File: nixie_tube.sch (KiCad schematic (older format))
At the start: 22 parts, among them J1 Conn_01x06_Male, J11 dc003a, J2 Conn_01x06_Female, J3 Conn_01x01_Male, J4 Conn_01x01_Female, Q1 SS8550, Q2 FQD5N60C, Q3 Q_NPN_BCE, Q4 AO3400, U1 MC34063

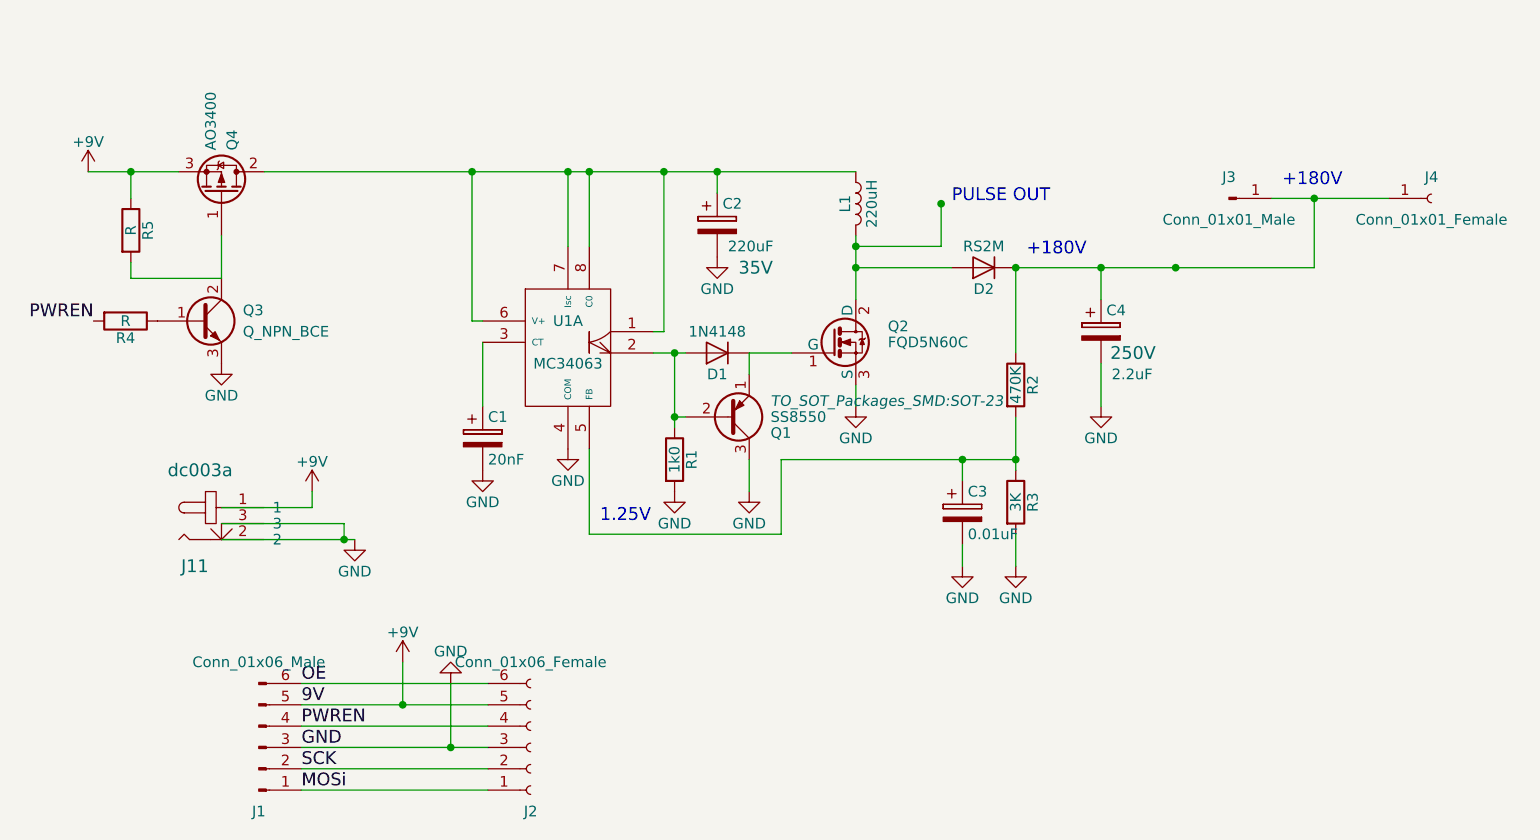
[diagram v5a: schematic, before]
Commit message: reallocate space for 4 m3 pins
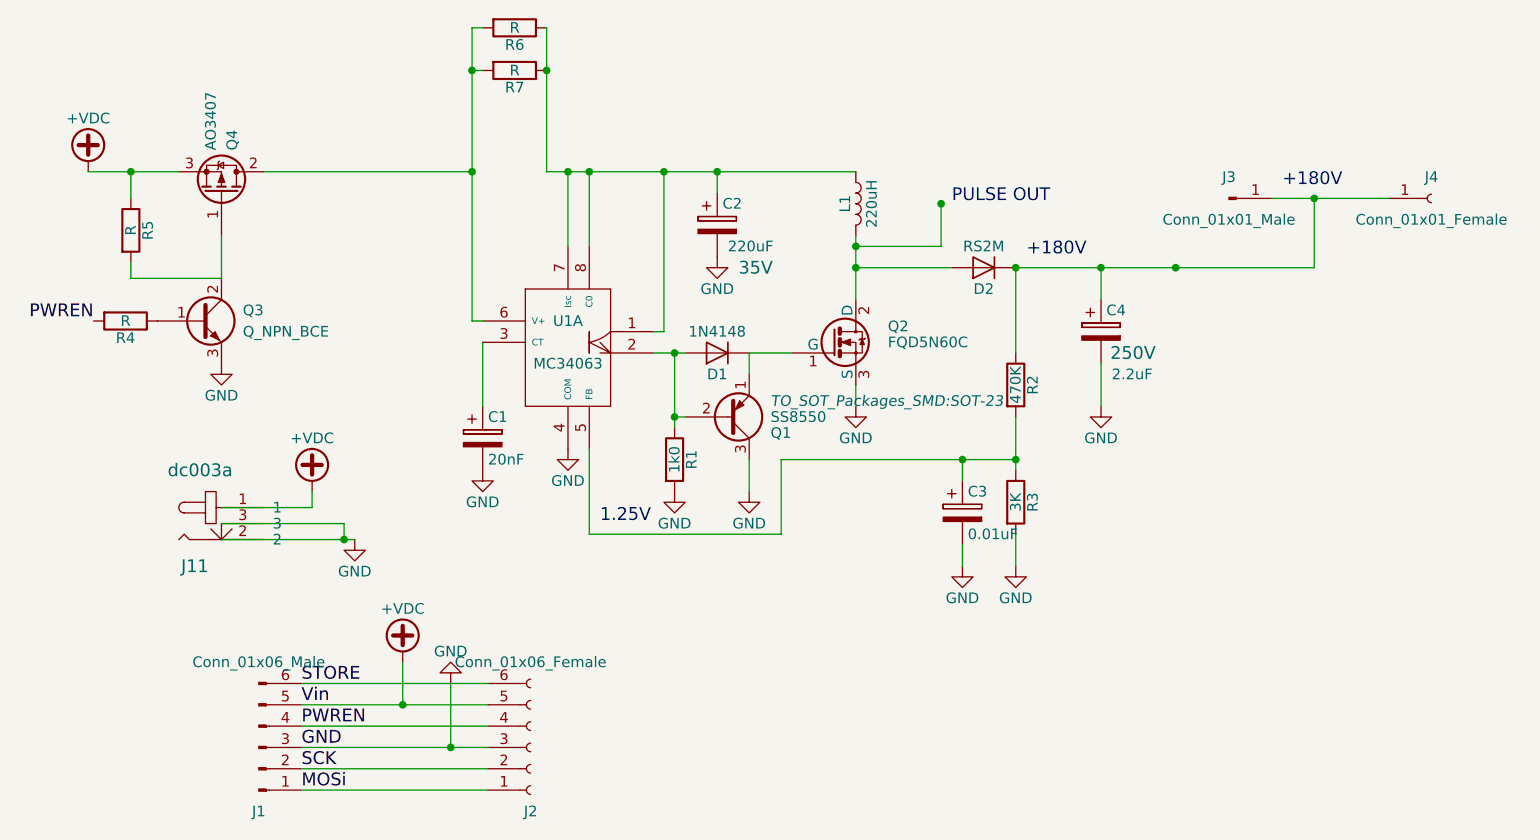
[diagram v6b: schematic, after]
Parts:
- added R6, R7: R, nixie-tube-fp:R_2512_0805, symbol R
- C4: footprint Capacitors_THT:CP_Radial_D8.0mm_P2.50mm -> nixie-tube-fp:CP_RADIAL_and_mlcc
- Q4: value AO3400 -> AO3407
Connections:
- net at C2.1, L1.1, U1.1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: now also R6.1, R7.1; no longer Q4.2 (D), U1.6 (V+)
- net +9V renamed +VDC
- net OE renamed STORE
- new net: Q4.2 (D), R6.2, R7.2, U1.6 (V+)
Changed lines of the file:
@@
 F 0 "C4" H 5975 3050 50  0000 L CNN
 F 1 "2.2uF" H 6000 2750 50  0000 L CNN
-F 2 "Capacitors_THT:CP_Radial_D8.0mm_P2.50mm" H 5988 2800 50  0001 C CNN
+F 2 "nixie-tube-fp:CP_RADIAL_and_mlcc" H 5988 2800 50  0001 C CNN
 F 3 "" H 5950 2950 50  0000 C CNN
 F 4 "250V" H 6100 2850 60  0000 C CNN "voltage"
@@
 $EndComp
 Text Label 2200 4700 0    60   ~ 0
-9V
+Vin
 Text Label 2200 4800 0    60   ~ 0
 PWREN
@@
 MOSi
 $Comp
-L +9V #PWR011
-U 1 1 59E5E8EF
-P 2250 3700
-F 0 "#PWR011" H 2250 3550 50  0001 C CNN
-F 1 "+9V" H 2250 3840 50  0000 C CNN
-F 2 "" H 2250 3700 50  0001 C CNN
-F 3 "" H 2250 3700 50  0001 C CNN
-	1    2250 3700
-	1    0    0    -1
-$EndComp
-Wire Wire Line
-	3450 2200 3450 2550
-Connection ~ 3450 2200
-Wire Wire Line
-	3850 2950 3900 2950
-Wire Wire Line
-	3900 2950 3900 2200
-Connection ~ 3550 2200
-Wire Wire Line
-	4150 2200 4150 2300
-Connection ~ 3900 2200
-Connection ~ 4150 2200
-Wire Wire Line
-	5550 2650 5550 3050
-Wire Wire Line
-	3550 3900 4450 3900
-Wire Wire Line
-	3550 3500 3550 3900
-Wire Wire Line
-	3850 3050 4000 3050
-Wire Wire Line
-	4300 3050 4300 3150
-Wire Wire Line
-	3950 3050 3950 3400
-Wire Wire Line
-	3950 3350 4000 3350
-Connection ~ 3950 3050
-Connection ~ 3950 3350
-Wire Wire Line
-	3050 3000 3050 3300
-Wire Wire Line
-	3000 2200 3000 2900
-Wire Wire Line
-	3000 2900 3050 2900
-Connection ~ 3000 2200
-Wire Wire Line
-	4800 3200 4800 3300
-Wire Wire Line
-	4300 3050 4500 3050
-Wire Wire Line
-	4800 2500 4800 2800
-Wire Wire Line
-	4800 2650 5250 2650
-Connection ~ 4800 2650
-Wire Wire Line
-	4800 2550 5200 2550
-Wire Wire Line
-	5200 2550 5200 2350
-Connection ~ 4800 2550
-Connection ~ 5200 2350
-Wire Wire Line
-	4450 3900 4450 3550
-Wire Wire Line
-	4450 3550 5550 3550
-Wire Wire Line
-	5550 3350 5550 3600
-Connection ~ 5550 3550
-Wire Wire Line
-	5300 3650 5300 3550
-Connection ~ 5300 3550
-Wire Wire Line
-	5300 3950 5300 4050
-Wire Wire Line
-	5550 2650 6950 2650
-Wire Wire Line
-	5950 2650 5950 2800
-Wire Wire Line
-	5950 3300 5950 3100
-Connection ~ 5950 2650
-Connection ~ 6300 2650
-Connection ~ 5550 2650
-Wire Wire Line
-	4300 3550 4300 3700
-Wire Wire Line
-	3550 2200 3550 2550
-Wire Wire Line
-	5550 4050 5550 3900
-Wire Wire Line
-	1825 3925 2450 3925
-Wire Wire Line
-	1825 3850 2400 3850
-Wire Wire Line
-	2400 3850 2400 3925
-Connection ~ 2400 3925
-Wire Wire Line
-	2200 4700 3075 4700
-Wire Wire Line
-	3075 4800 2200 4800
-Wire Wire Line
-	2200 4900 3075 4900
-Wire Wire Line
-	3075 5000 2200 5000
-Wire Wire Line
-	2200 5100 3075 5100
-Wire Wire Line
-	2250 3775 2250 3700
-$Comp
-L +9V #PWR012
-U 1 1 59E5EF02
-P 2675 4500
-F 0 "#PWR012" H 2675 4350 50  0001 C CNN
-F 1 "+9V" H 2675 4640 50  0000 C CNN
-F 2 "" H 2675 4500 50  0001 C CNN
-F 3 "" H 2675 4500 50  0001 C CNN
-	1    2675 4500
-	1    0    0    -1
-$EndComp
-Wire Wire Line
-	2675 4500 2675 4700
-Connection ~ 2675 4700
-$Comp
-L GND #PWR013
+L GND #PWR011
 U 1 1 59E5EFC2
 P 2900 4600
-F 0 "#PWR013" H 2900 4350 50  0001 C CNN
+F 0 "#PWR011" H 2900 4350 50  0001 C CNN
 F 1 "GND" H 2900 4450 50  0000 C CNN
 F 2 "" H 2900 4600 50  0001 C CNN
@@
 	-1   0    0    1
 $EndComp
-Wire Wire Line
-	2900 4900 2900 4600
-Connection ~ 2900 4900
-Wire Wire Line
-	6950 2650 6950 2325
-Wire Wire Line
-	6750 2325 7300 2325
-Connection ~ 6950 2325
 Text Notes 6800 2275 0    60   ~ 0
 +180V
-Wire Wire Line
-	2025 2200 4800 2200
-$Comp
-L +9V #PWR014
-U 1 1 59E606F5
-P 1200 2200
-F 0 "#PWR014" H 1200 2050 50  0001 C CNN
-F 1 "+9V" H 1200 2340 50  0000 C CNN
-F 2 "" H 1200 2200 50  0001 C CNN
-F 3 "" H 1200 2200 50  0001 C CNN
-	1    1200 2200
-	1    0    0    -1
-$EndComp
-Wire Wire Line
-	2250 3775 1825 3775
 $Comp
 L R R5
@@
 	1    0    0    -1
 $EndComp
-Wire Wire Line
-	1200 2200 1625 2200
-Wire Wire Line
-	1400 2325 1400 2200
-Connection ~ 1400 2200
-Wire Wire Line
-	1400 2625 1400 2700
-Wire Wire Line
-	1400 2700 1825 2700
-Wire Wire Line
-	1825 2700 1825 2500
 $Comp
 L R R4
@@
 PWREN
 $Comp
-L GND #PWR015
+L GND #PWR012
 U 1 1 59E613BB
 P 1825 3100
-F 0 "#PWR015" H 1825 2850 50  0001 C CNN
+F 0 "#PWR012" H 1825 2850 50  0001 C CNN
 F 1 "GND" H 1825 2950 50  0000 C CNN
 F 2 "" H 1825 3100 50  0001 C CNN
@@
 P 1825 2300
 F 0 "Q4" H 2025 2350 50  0000 L CNN
-F 1 "AO3400" H 2025 2250 50  0000 L CNN
+F 1 "AO3407" H 2025 2250 50  0000 L CNN
 F 2 "TO_SOT_Packages_SMD:SOT-23" H 2025 2400 50  0001 C CNN
 F 3 "" H 1825 2300 50  0001 C CNN
@@
 	1    0    0    1
 $EndComp
+Text Label 2200 4600 0    60   ~ 0
+STORE
+$Comp
+L +VDC #PWR013
+U 1 1 5A0B6931
+P 2675 4500
+F 0 "#PWR013" H 2675 4400 50  0001 C CNN
+F 1 "+VDC" H 2675 4750 50  0000 C CNN
+F 2 "" H 2675 4500 50  0001 C CNN
+F 3 "" H 2675 4500 50  0001 C CNN
+	1    2675 4500
+	1    0    0    -1
+$EndComp
+$Comp
+L +VDC #PWR014
+U 1 1 5A0B699B
+P 2250 3700
+F 0 "#PWR014" H 2250 3600 50  0001 C CNN
+F 1 "+VDC" H 2250 3950 50  0000 C CNN
+F 2 "" H 2250 3700 50  0001 C CNN
+F 3 "" H 2250 3700 50  0001 C CNN
+	1    2250 3700
+	1    0    0    -1
+$EndComp
+$Comp
+L +VDC #PWR015
+U 1 1 5A0B7EB4
+P 1200 2200
+F 0 "#PWR015" H 1200 2100 50  0001 C CNN
+F 1 "+VDC" H 1200 2450 50  0000 C CNN
+F 2 "" H 1200 2200 50  0001 C CNN
+F 3 "" H 1200 2200 50  0001 C CNN
+	1    1200 2200
+	1    0    0    -1
+$EndComp
+$Comp
+L R R7
+U 1 1 5A0BB77E
+P 3200 1725
+F 0 "R7" V 3280 1725 50  0000 C CNN
+F 1 "R" V 3200 1725 50  0000 C CNN
+F 2 "nixie-tube-fp:R_2512_0805" V 3130 1725 50  0001 C CNN
+F 3 "" H 3200 1725 50  0001 C CNN
+	1    3200 1725
+	0    1    1    0
+$EndComp
+$Comp
+L R R6
+U 1 1 5A0BB87E
+P 3200 1525
+F 0 "R6" V 3280 1525 50  0000 C CNN
+F 1 "R" V 3200 1525 50  0000 C CNN
+F 2 "nixie-tube-fp:R_2512_0805" V 3130 1525 50  0001 C CNN
+F 3 "" H 3200 1525 50  0001 C CNN
+	1    3200 1525
+	0    1    1    0
+$EndComp
+Wire Wire Line
+	3450 2200 3450 2550
+Connection ~ 3450 2200
+Wire Wire Line
+	3850 2950 3900 2950
+Wire Wire Line
+	3900 2950 3900 2200
+Connection ~ 3550 2200
+Wire Wire Line
+	4150 2200 4150 2300
+Connection ~ 3900 2200
+Connection ~ 4150 2200
+Wire Wire Line
+	5550 2650 5550 3050
+Wire Wire Line
+	3550 3900 4450 3900
+Wire Wire Line
+	3550 3500 3550 3900
+Wire Wire Line
+	3850 3050 4000 3050
+Wire Wire Line
+	4300 3050 4300 3150
+Wire Wire Line
+	3950 3050 3950 3400
+Wire Wire Line
+	3950 3350 4000 3350
+Connection ~ 3950 3050
+Connection ~ 3950 3350
+Wire Wire Line
+	3050 3000 3050 3300
+Wire Wire Line
+	3000 1525 3000 2900
+Wire Wire Line
+	3000 2900 3050 2900
+Connection ~ 3000 2200
+Wire Wire Line
+	4800 3200 4800 3300
+Wire Wire Line
+	4300 3050 4500 3050
+Wire Wire Line
+	4800 2500 4800 2800
+Wire Wire Line
+	4800 2650 5250 2650
+Connection ~ 4800 2650
+Wire Wire Line
+	4800 2550 5200 2550
+Wire Wire Line
+	5200 2550 5200 2350
+Connection ~ 4800 2550
+Connection ~ 5200 2350
+Wire Wire Line
+	4450 3900 4450 3550
+Wire Wire Line
+	4450 3550 5550 3550
+Wire Wire Line
+	5550 3350 5550 3600
+Connection ~ 5550 3550
+Wire Wire Line
+	5300 3650 5300 3550
+Connection ~ 5300 3550
+Wire Wire Line
+	5300 3950 5300 4050
+Wire Wire Line
+	5550 2650 6950 2650
+Wire Wire Line
+	5950 2650 5950 2800
+Wire Wire Line
+	5950 3300 5950 3100
+Connection ~ 5950 2650
+Connection ~ 6300 2650
+Connection ~ 5550 2650
+Wire Wire Line
+	4300 3550 4300 3700
+Wire Wire Line
+	3550 2200 3550 2550
+Wire Wire Line
+	5550 4050 5550 3900
+Wire Wire Line
+	1825 3925 2450 3925
+Wire Wire Line
+	1825 3850 2400 3850
+Wire Wire Line
+	2400 3850 2400 3925
+Connection ~ 2400 3925
+Wire Wire Line
+	2200 4700 3075 4700
+Wire Wire Line
+	3075 4800 2200 4800
+Wire Wire Line
+	2200 4900 3075 4900
+Wire Wire Line
+	3075 5000 2200 5000
+Wire Wire Line
+	2200 5100 3075 5100
+Wire Wire Line
+	2250 3775 2250 3700
+Wire Wire Line
+	2675 4500 2675 4700
+Connection ~ 2675 4700
+Wire Wire Line
+	2900 4900 2900 4600
+Connection ~ 2900 4900
+Wire Wire Line
+	6950 2650 6950 2325
+Wire Wire Line
+	6750 2325 7300 2325
+Connection ~ 6950 2325
+Wire Wire Line
+	2250 3775 1825 3775
+Wire Wire Line
+	1200 2200 1625 2200
+Wire Wire Line
+	1400 2325 1400 2200
+Connection ~ 1400 2200
+Wire Wire Line
+	1400 2625 1400 2700
+Wire Wire Line
+	1400 2700 1825 2700
+Wire Wire Line
+	1825 2700 1825 2500
 Wire Wire Line
 	2200 4600 3075 4600
-Text Label 2200 4600 0    60   ~ 0
-OE
+Wire Wire Line
+	3050 1725 3000 1725
+Wire Wire Line
+	3050 1525 3000 1525
+Connection ~ 3000 1725
+Wire Wire Line
+	3350 1525 3350 2200
+Connection ~ 3350 1725
+Wire Wire Line
+	3350 2200 4800 2200
+Wire Wire Line
+	2025 2200 3000 2200
 $EndSCHEMATC

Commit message: fixed pin number not same with actual numbering of component
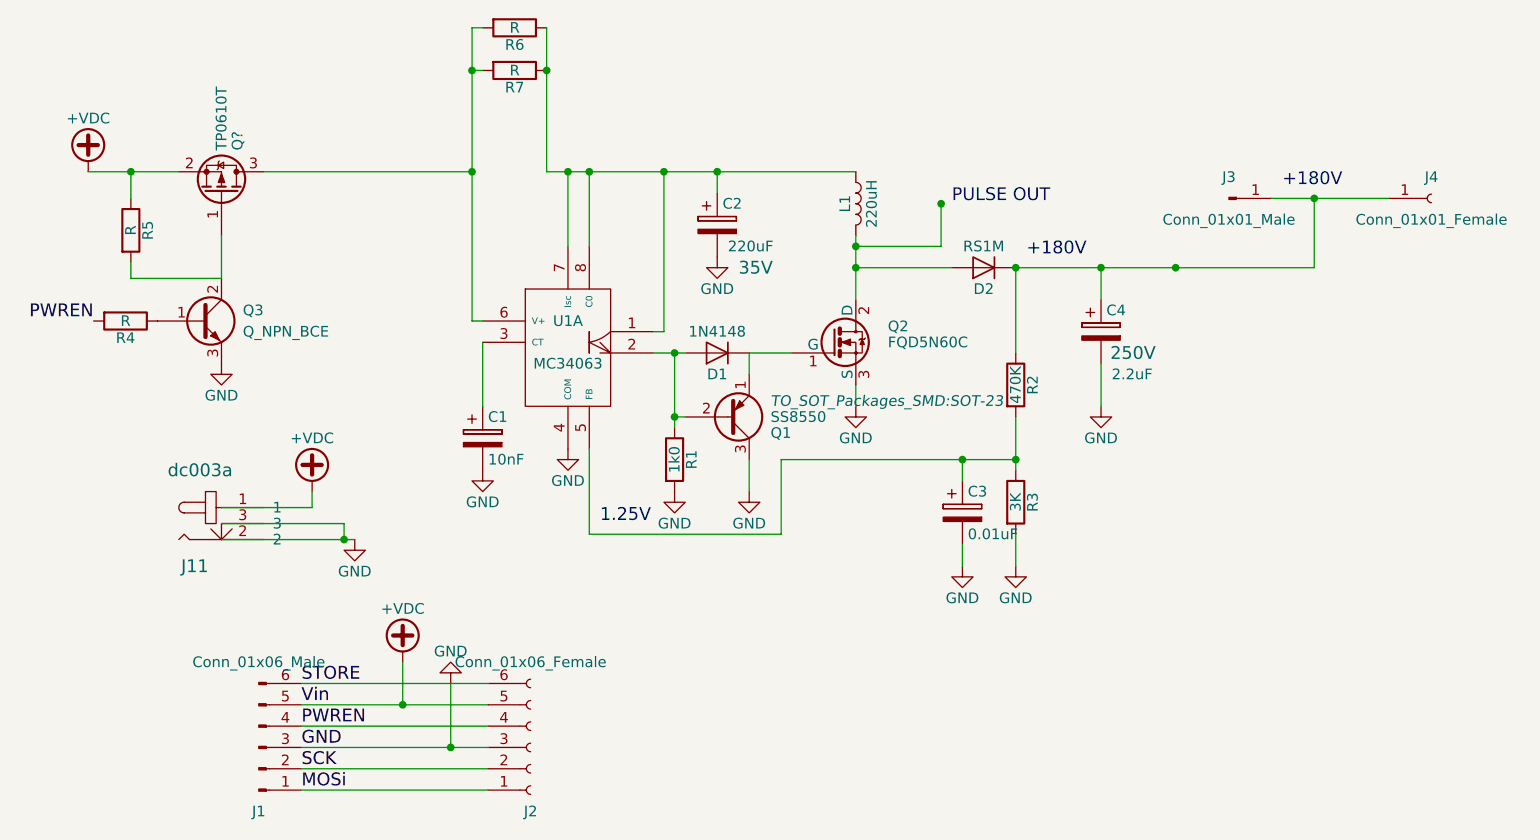
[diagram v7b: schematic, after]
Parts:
- removed Q4: AO3407, TO_SOT_Packages_SMD:SOT-23, symbol Q_PMOS_GDS
- added Q?: TP0610T, TO_SOT_Packages_SMD:SOT-23, symbol TP0610T
- C1: value 20nF -> 10nF
- D2: value RS2M -> RS1M
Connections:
- net +VDC: now also Q?.2 (S)
- net at R6.2, R7.2, U1.6 (V+): now also Q?.3 (D)
- net at Q3.2 (C), R5.2: now also Q?.1 (G)
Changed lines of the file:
@@
 P 5400 2650
 F 0 "D2" H 5400 2750 50  0000 C CNN
-F 1 "RS2M" H 5400 2550 50  0000 C CNN
+F 1 "RS1M" H 5400 2550 50  0000 C CNN
 F 2 "Diodes_SMD:D_SMA" H 5400 2650 50  0001 C CNN
 F 3 "" H 5400 2650 50  0000 C CNN
@@
 P 3050 3450
 F 0 "C1" H 3075 3550 50  0000 L CNN
-F 1 "20nF" H 3075 3350 50  0000 L CNN
+F 1 "10nF" H 3075 3350 50  0000 L CNN
 F 2 "Capacitors_SMD:C_0603" H 3088 3300 50  0001 C CNN
 F 3 "" H 3050 3450 50  0000 C CNN
@@
 $EndComp
 $Comp
-L Q_PMOS_GDS Q4
-U 1 1 59E61F36
-P 1825 2300
-F 0 "Q4" H 2025 2350 50  0000 L CNN
-F 1 "AO3407" H 2025 2250 50  0000 L CNN
-F 2 "TO_SOT_Packages_SMD:SOT-23" H 2025 2400 50  0001 C CNN
-F 3 "" H 1825 2300 50  0001 C CNN
-	1    1825 2300
-	0    1    -1   0
-$EndComp
-$Comp
 L Conn_01x06_Male J1
 U 1 1 59F6FE01
@@
 Wire Wire Line
 	2025 2200 3000 2200
+$Comp
+L TP0610T Q?
+U 1 1 5A0C79BF
+P 1825 2300
+F 0 "Q?" H 2025 2375 50  0000 L CNN
+F 1 "TP0610T" H 2025 2300 50  0000 L CNN
+F 2 "TO_SOT_Packages_SMD:SOT-23" H 2025 2225 50  0001 L CIN
+F 3 "" H 1825 2300 50  0001 L CNN
+	1    1825 2300
+	0    1    -1   0
+$EndComp
 $EndSCHEMATC

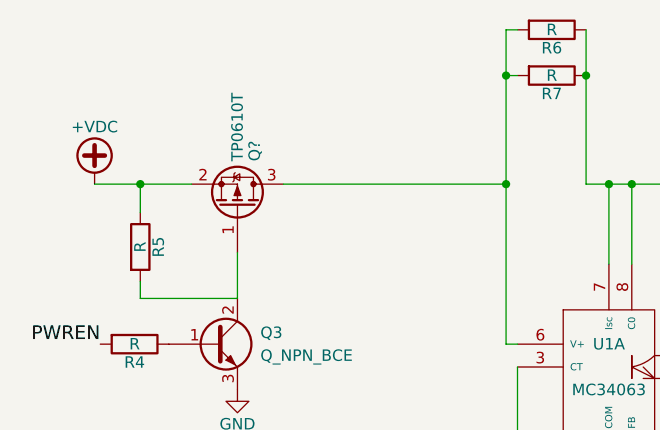
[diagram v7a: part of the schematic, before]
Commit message: extend ao3407 pad for making soldering easier when we dont want HV switching
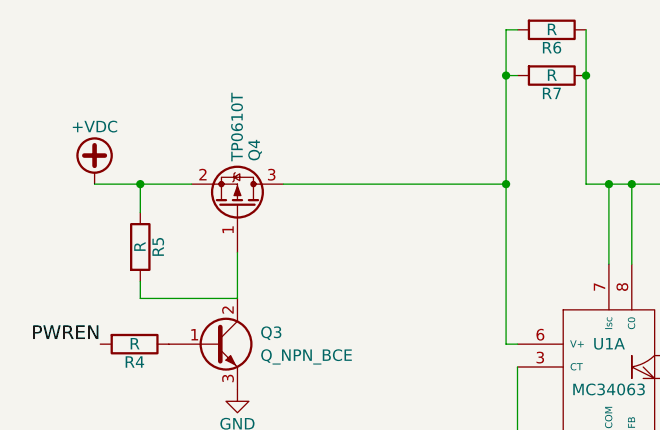
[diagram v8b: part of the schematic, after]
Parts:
- Q4: renamed from Q?; footprint TO_SOT_Packages_SMD:SOT-23 -> nixie-tube-fp:SOT-23-alt_solder_on2_3
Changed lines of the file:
@@
 	2025 2200 3000 2200
 $Comp
-L TP0610T Q?
+L TP0610T Q4
 U 1 1 5A0C79BF
 P 1825 2300
-F 0 "Q?" H 2025 2375 50  0000 L CNN
+F 0 "Q4" H 2025 2375 50  0000 L CNN
 F 1 "TP0610T" H 2025 2300 50  0000 L CNN
-F 2 "TO_SOT_Packages_SMD:SOT-23" H 2025 2225 50  0001 L CIN
+F 2 "nixie-tube-fp:SOT-23-alt_solder_on2_3" H 2025 2225 50  0001 L CIN
 F 3 "" H 1825 2300 50  0001 L CNN
 	1    1825 2300
